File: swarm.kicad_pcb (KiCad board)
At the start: 2 copper layers, 23 parts, among them P1 USB_OTG, P2 CONN_02X20, SW1 SW_PUSH, U1 STM32F103RETx, U2 LM3671MF-3.3, Y1 Crystal

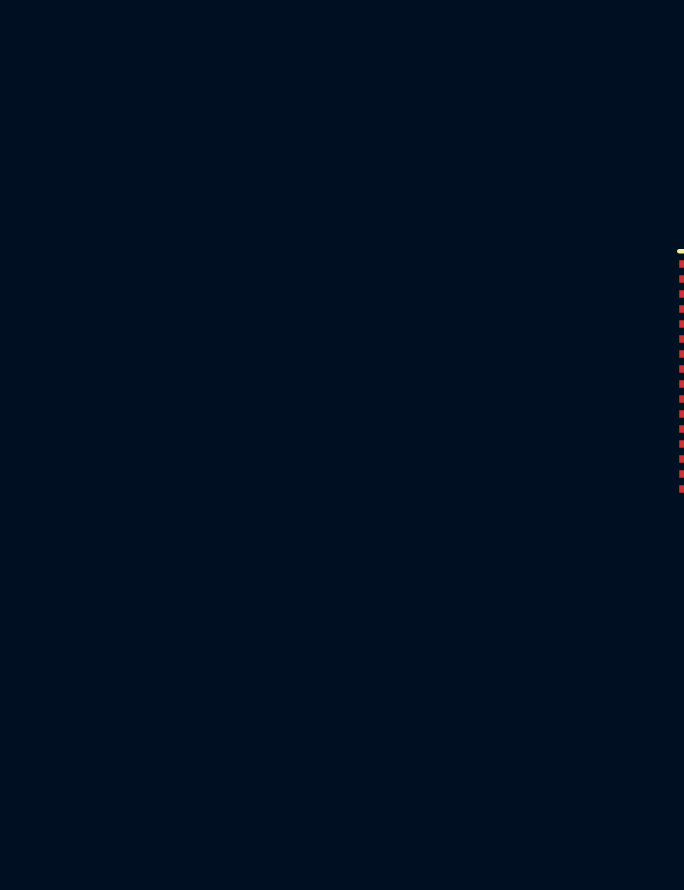
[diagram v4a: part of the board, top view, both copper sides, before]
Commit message: Adds Serial Wire Debug connector (5 pins) Sets up PCB layers based on Osh Park's Layer setup
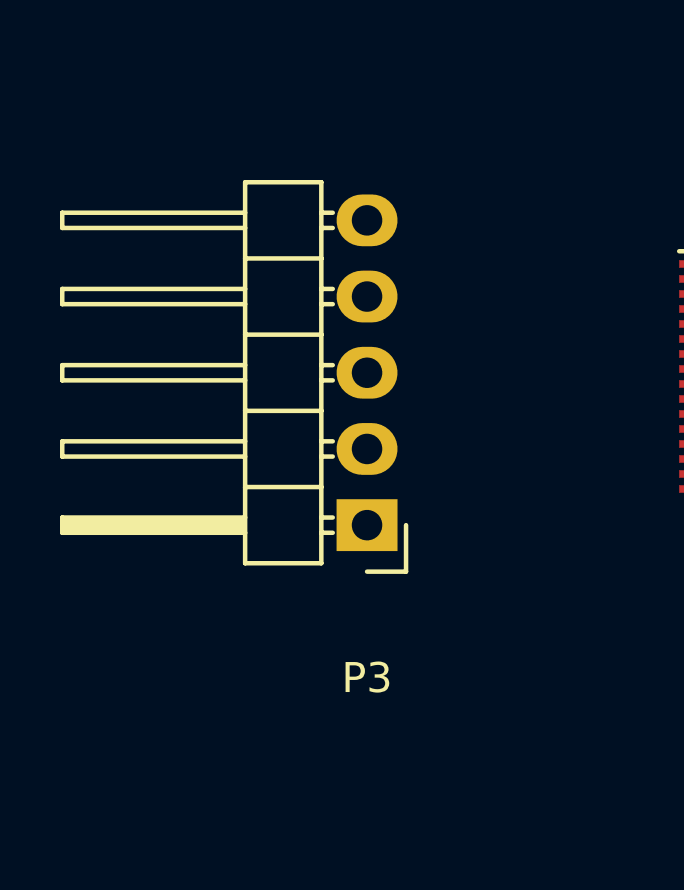
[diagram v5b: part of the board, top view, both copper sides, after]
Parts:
- added P3: CONN_01X05, Pin_Headers:Pin_Header_Angled_1x05, F.Cu at (67.0, 117.3)
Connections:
- net /+3.3V renamed /LCD_VCC
- net Net-(C4-Pad1) renamed /NRST
- U1 pad 46: Net-(U1-Pad46) -> /SWDIO
- U1 pad 49: Net-(U1-Pad49) -> /SWCLK

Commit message: Updates to Design Rules and board thicknes based on Osh Park's setup
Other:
- net class Default: clearance 0.2 -> 0.1524; trace_width 0.25 -> 0.1524; via_dia 0.6 -> 0.6858; via_drill 0.4 -> 0.3302
- rule trace_clearance: 0.2 -> 0.1524
- rule trace_min: 0.2 -> 0.1524
- rule via_min_drill: 0.3 -> 0.3302
- rule via_min_size: 0.4 -> 0.6858
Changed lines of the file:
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@@
     (no_connects 88)
     (area 0 0 0 0)
-    (thickness 1.6)
+    (thickness 1.6002)
     (drawings 0)
     (tracks 0)
@@
   )
   (setup
-    (last_trace_width 0.25)
-    (trace_clearance 0.2)
+    (last_trace_width 0.1524)
+    (trace_clearance 0.1524)
     (zone_clearance 0.508)
     (zone_45_only no)
-    (trace_min 0.2)
+    (trace_min 0.1524)
     (segment_width 0.2)
     (edge_width 0.15)
-    (via_size 0.6)
-    (via_drill 0.4)
-    (via_min_size 0.4)
-    (via_min_drill 0.3)
-    (uvia_size 0.3)
-    (uvia_drill 0.1)
+    (via_size 0.6858)
+    (via_drill 0.3302)
+    (via_min_size 0.6858)
+    (via_min_drill 0.3302)
+    (uvia_size 0.762)
+    (uvia_drill 0.508)
     (uvias_allowed no)
-    (uvia_min_size 0.2)
-    (uvia_min_drill 0.1)
+    (uvia_min_size 0)
+    (uvia_min_drill 0)
     (pcb_text_width 0.3)
     (pcb_text_size 1.5 1.5)
@@
   (net 86 /SWCLK)
   (net_class Default "This is the default net class."
-    (clearance 0.2)
-    (trace_width 0.25)
-    (via_dia 0.6)
-    (via_drill 0.4)
-    (uvia_dia 0.3)
-    (uvia_drill 0.1)
+    (clearance 0.1524)
+    (trace_width 0.1524)
+    (via_dia 0.6858)
+    (via_drill 0.3302)
+    (uvia_dia 0.762)
+    (uvia_drill 0.508)
     (add_net +3V3)
     (add_net /+3.3V)

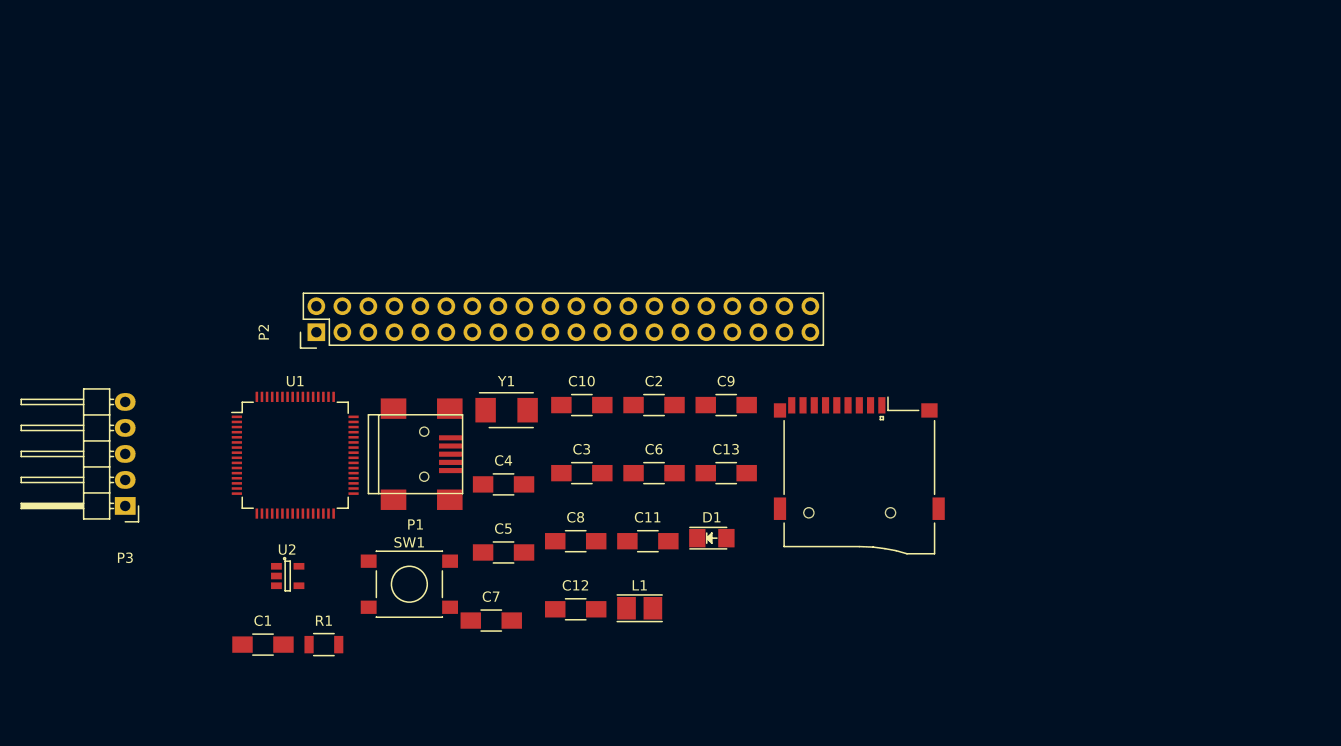
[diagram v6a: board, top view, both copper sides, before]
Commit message: Replaces 0603 components with smaller fooprint Regenerated net file and imported in pcbnew
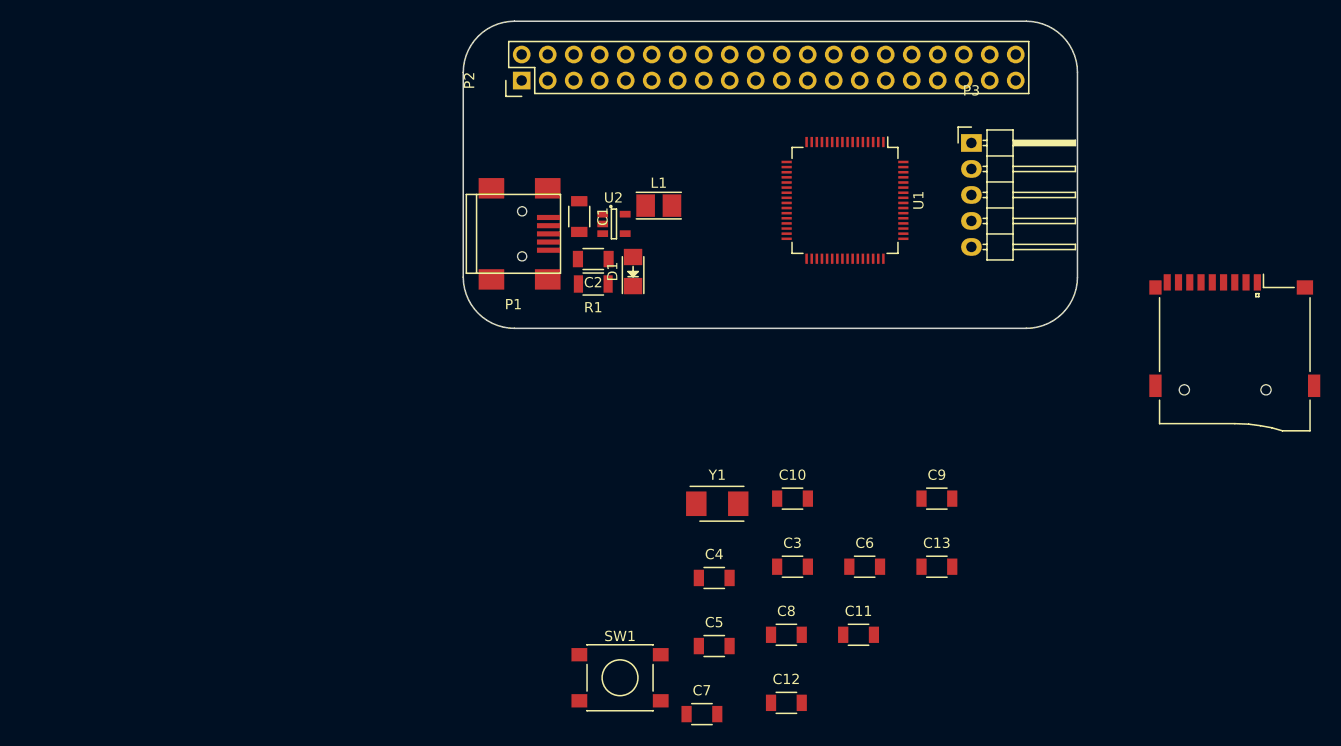
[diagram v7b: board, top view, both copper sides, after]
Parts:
- C1, C10, C11, C12, C13, C2, C3, C4, C5, C6, C7, C8, C9: footprint Capacitors_SMD:C_1206_HandSoldering -> Capacitors_SMD:C_1206
- moved P3 89.9 mm to (149.6, 81.9), turned to 0 degrees
- moved U1 59.2 mm to (137.3, 87.5), turned to 270 degrees
- moved C1 52.0 mm to (111.3, 89.1), turned to 270 degrees
- moved U2 46.9 mm to (114.7, 89.8)
- moved R1 44.0 mm to (112.7, 95.7), turned to 180 degrees
- moved L1 39.4 mm to (119.1, 88.0)
- moved XS1 38.6 mm to (175.4, 106.0)
- moved P2 31.7 mm to (105.7, 75.8)
- moved D1 27.2 mm to (116.6, 94.5), turned to 90 degrees
- moved P1 23.6 mm to (104.9, 90.8)
- moved C11 22.5 mm to (138.6, 129.9)
- moved C13 22.5 mm to (146.3, 123.3)
- moved C9 22.5 mm to (146.3, 116.6)
- moved C12 22.5 mm to (131.6, 136.6)
- moved C7 22.5 mm to (123.3, 137.7)
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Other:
- board outline added: 60 x 30 mm

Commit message: Adds APA102 SPI RGB LED Updates schematic references and links docoupling capacitors based on input pin
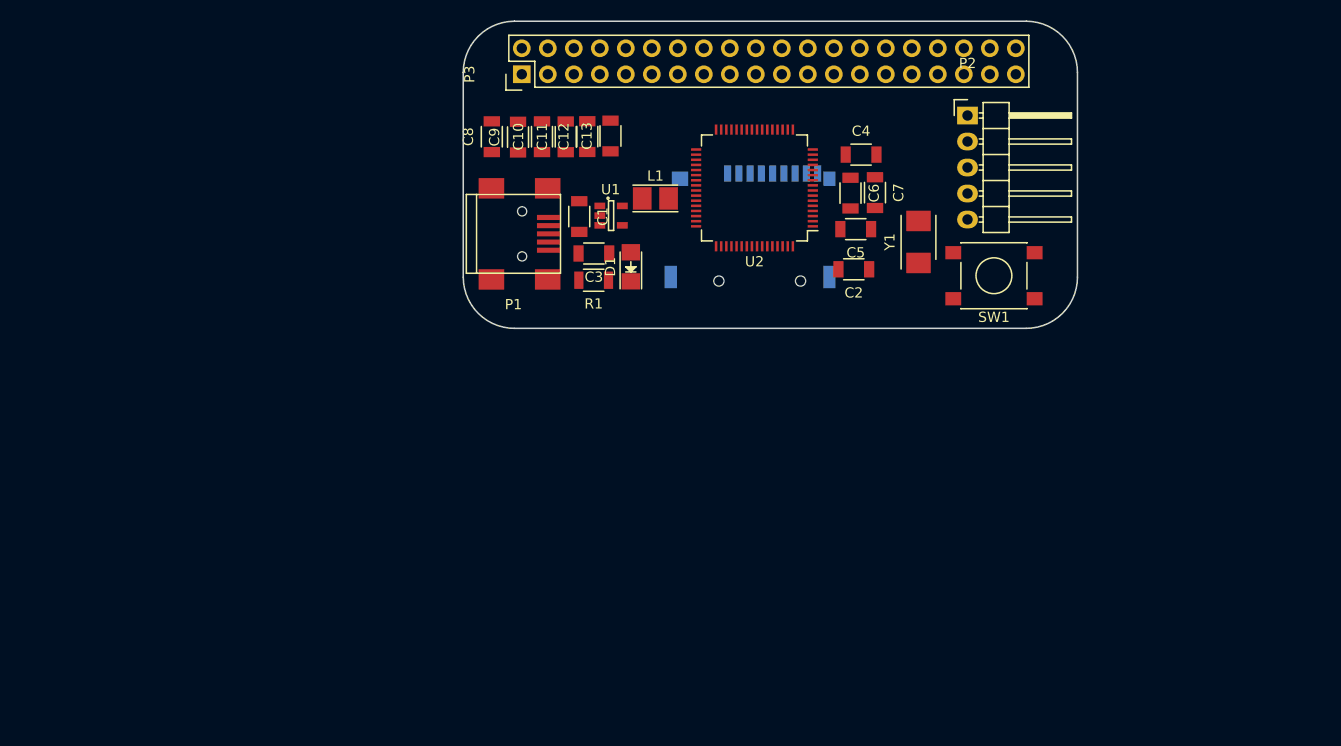
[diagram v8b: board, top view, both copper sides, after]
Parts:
- C2: value 22uF -> C
- C3: value C -> 22uF
- C6: value 1u -> 100n
- C7: value 10u -> 1u
- C8: value 100n -> 10u
- P2: value CONN_02X20 -> CONN_01X05; footprint Pin_Headers:Pin_Header_Straight_2x20 -> Pin_Headers:Pin_Header_Angled_1x05
- P3: value CONN_01X05 -> CONN_02X20; footprint Pin_Headers:Pin_Header_Angled_1x05 -> Pin_Headers:Pin_Header_Straight_2x20
- U1: value STM32F103RETx -> LM3671MF-3.3; footprint Housings_QFP:LQFP-64_10x10mm_Pitch0.5mm -> TO_SOT_Packages_SMD:SOT-23-5
- U2: value LM3671MF-3.3 -> STM32F103RETx; footprint TO_SOT_Packages_SMD:SOT-23-5 -> Housings_QFP:LQFP-64_10x10mm_Pitch0.5mm
- XS1: moved to B.Cu
- moved C12 58.6 mm to (112.1, 81.3), turned to 90 degrees
- moved C8 56.5 mm to (102.8, 81.3), turned to 90 degrees
- moved C11 56.4 mm to (110.0, 81.3), turned to 90 degrees
- moved C9 54.0 mm to (105.3, 81.3), turned to 90 degrees
- moved C7 53.7 mm to (140.2, 86.7), turned to 270 degrees
- moved SW1 53.6 mm to (151.8, 94.9), turned to 180 degrees
- moved C13 52.8 mm to (114.4, 81.2), turned to 90 degrees
- moved XS1 48.5 mm to (128.0, 95.4), turned to 180 degrees
- moved P3 44.4 mm to (105.7, 75.2), turned to 90 degrees
- moved C4 43.8 mm to (138.9, 83.0)
- moved P2 43.7 mm to (149.3, 79.2), turned to 0 degrees
- moved C5 43.0 mm to (138.3, 90.3), turned to 180 degrees
- moved C10 43.0 mm to (107.7, 81.3), turned to 90 degrees
- moved C6 36.5 mm to (137.8, 86.8), turned to 270 degrees
- moved C3 36.2 mm to (112.8, 92.7), turned to 180 degrees
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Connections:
- C2 pad 1: +3V3 -> Net-(C2-Pad1)
- C3 pad 1: Net-(C3-Pad1) -> +3V3
- P2 pad 1: GND -> /NRST
- P2 pad 2: /LCD_D0 -> /SWDIO
- P2 pad 3: /LCD_VCC -> GND
- P2 pad 4: /LCD_D1 -> /SWCLK
- P2 pad 5: Net-(P2-Pad5) -> /+3.3V
- P3 pad 1: /NRST -> GND
- P3 pad 2: /SWDIO -> /LCD_D0
- P3 pad 3: GND -> /LCD_VCC
- P3 pad 4: /SWCLK -> /LCD_D1
- P3 pad 5: /+3.3V -> Net-(P3-Pad5)
- U1 pad 1: +3V3 -> VCC
- U1 pad 2: Net-(U1-Pad2) -> GND
- U1 pad 3: Net-(U1-Pad3) -> VCC
- U1 pad 4: Net-(U1-Pad4) -> +3V3
- U1 pad 5: Net-(C3-Pad1) -> Net-(L1-Pad1)
- U2 pad 1: VCC -> +3V3
- U2 pad 2: GND -> Net-(U2-Pad2)
- U2 pad 3: VCC -> Net-(U2-Pad3)
- U2 pad 4: +3V3 -> Net-(U2-Pad4)
- U2 pad 5: Net-(L1-Pad1) -> Net-(C2-Pad1)
- Y1 pad 1: Net-(C3-Pad1) -> Net-(C2-Pad1)
